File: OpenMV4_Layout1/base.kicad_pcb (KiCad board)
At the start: 4 copper layers, 35.6 x 44.5 mm, 57 parts, among them M1 9774030243R, M2 9774030243R, Q1 BSS138, Q2 Si2301BDS, U1 STM32H743VIT6, U5 TPS731XX, U8 PAM2305AABADJ, X1 MF-CON-MICROUSB-RIGHT, X2 USD-1040310811, X3 DF12-36-DS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

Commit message: Swapped image sensor connector to opposite side
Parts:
- added LOGO1: OSHW_LOGO_FILLX0100-NT, base:OSHW_FILLX100_NOTEXT, F.Cu at (182.9, 90.2)
- X3: moved to B.Cu

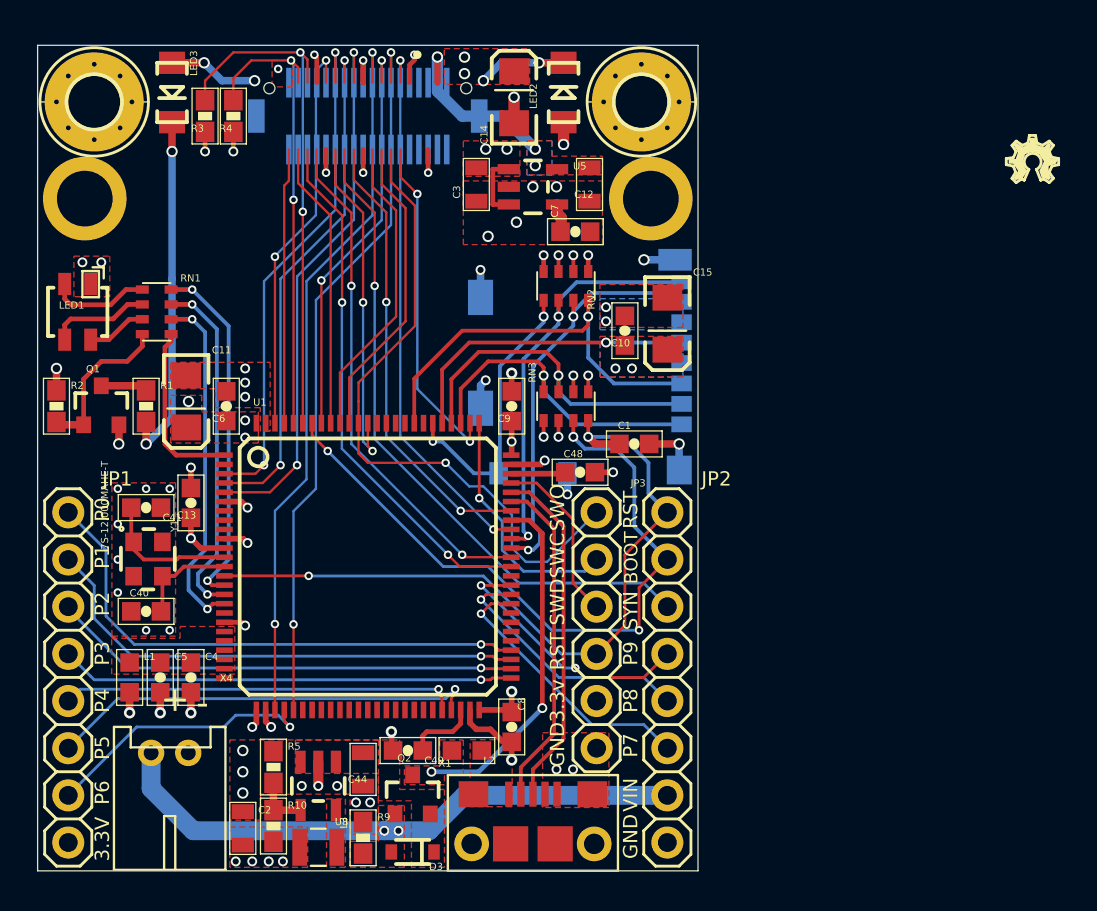
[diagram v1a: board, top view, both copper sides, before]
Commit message: Found diffs MV3 to MV4 for direct mount
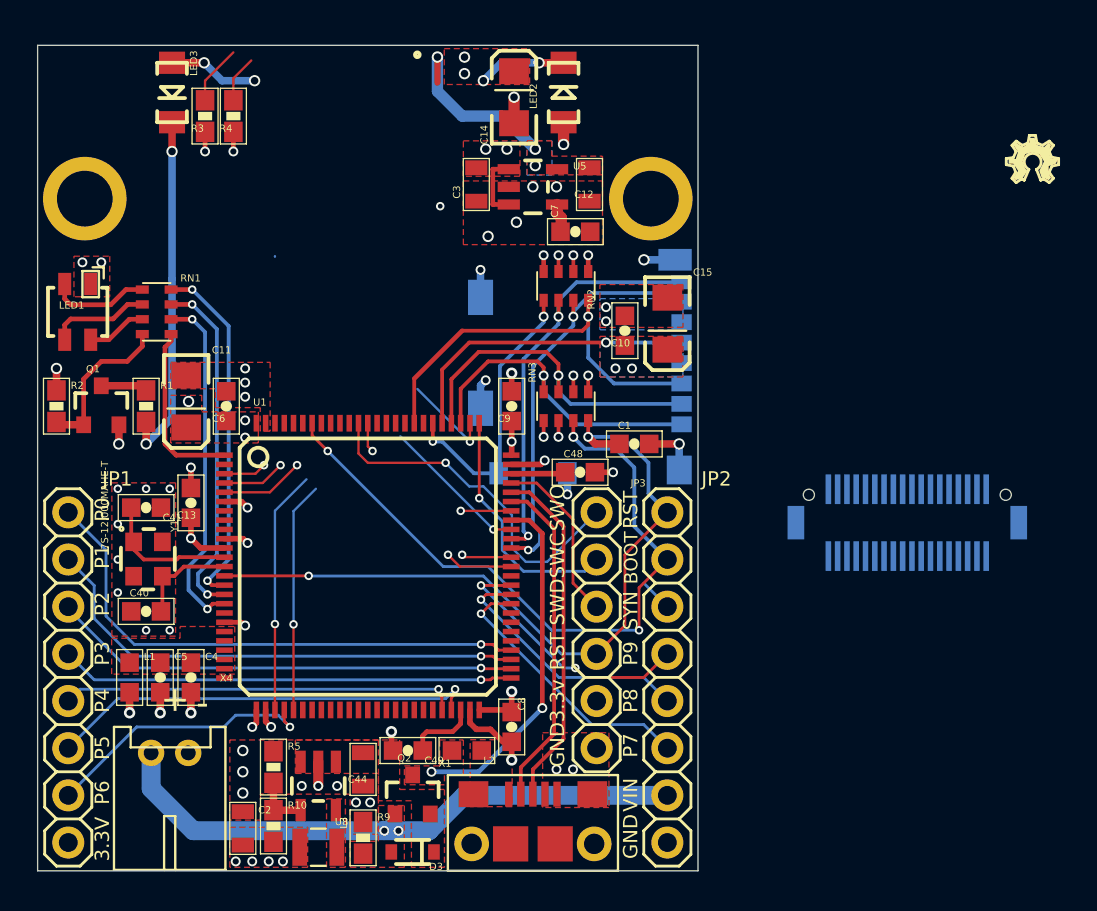
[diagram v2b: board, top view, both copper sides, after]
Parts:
- removed H1, H2: MOUNT-PAD-ROUND2.8, base:2,8-PAD
- moved X3 36.4 mm to (177.6, 108.5)
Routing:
- net /DCMI_FSIN: track 35.8 -> 1.80 mm, vias 1 -> 0
- net /DCMI_PCLK: track 39.2 -> 12.4 mm, vias 2 -> 1
- net /DCMI_HSYNC: track 39.2 -> 13.1 mm, vias 2 -> 1
- net /DCMI_D4: track 27.8 -> 2.32 mm, vias 2 -> 1
- net /I2C1_SCL: track 28.6 -> 3.21 mm, vias 2 -> 0
- net /DCMI_D7: track 29.6 -> 4.52 mm, vias 2 -> 1
- net /DCMI_D1: track 27.8 -> 2.70 mm, vias 2 -> 1
- net /DCMI_D0: track 28.6 -> 3.67 mm, vias 2 -> 1
- net /DCMI_D6: track 27.8 -> 3.42 mm, vias 2 -> 1
- net /I2C1_SDA: track 25.6 -> 2.55 mm, vias 2 -> 0
- net /DCMI_VSYNC: track 22.1 -> 0.00 mm, vias 2 -> 0
- net /DCMI_RST: track 24.6 -> 2.72 mm, vias 2 -> 1
- net /DCMI_D3: track 21.9 -> 0.03 mm, vias 2 -> 0
- net /DCMI_CLK: track 29.5 -> 8.05 mm, vias 2 -> 1
- net /DCMI_PWDN: track 18.7 -> 1.60 mm, vias 2 -> 1
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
